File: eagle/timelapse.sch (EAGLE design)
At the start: 21 parts, among them Q1 200mA/40V, Q2 60V/32A/35mΩ, U2 TSR_1-2450

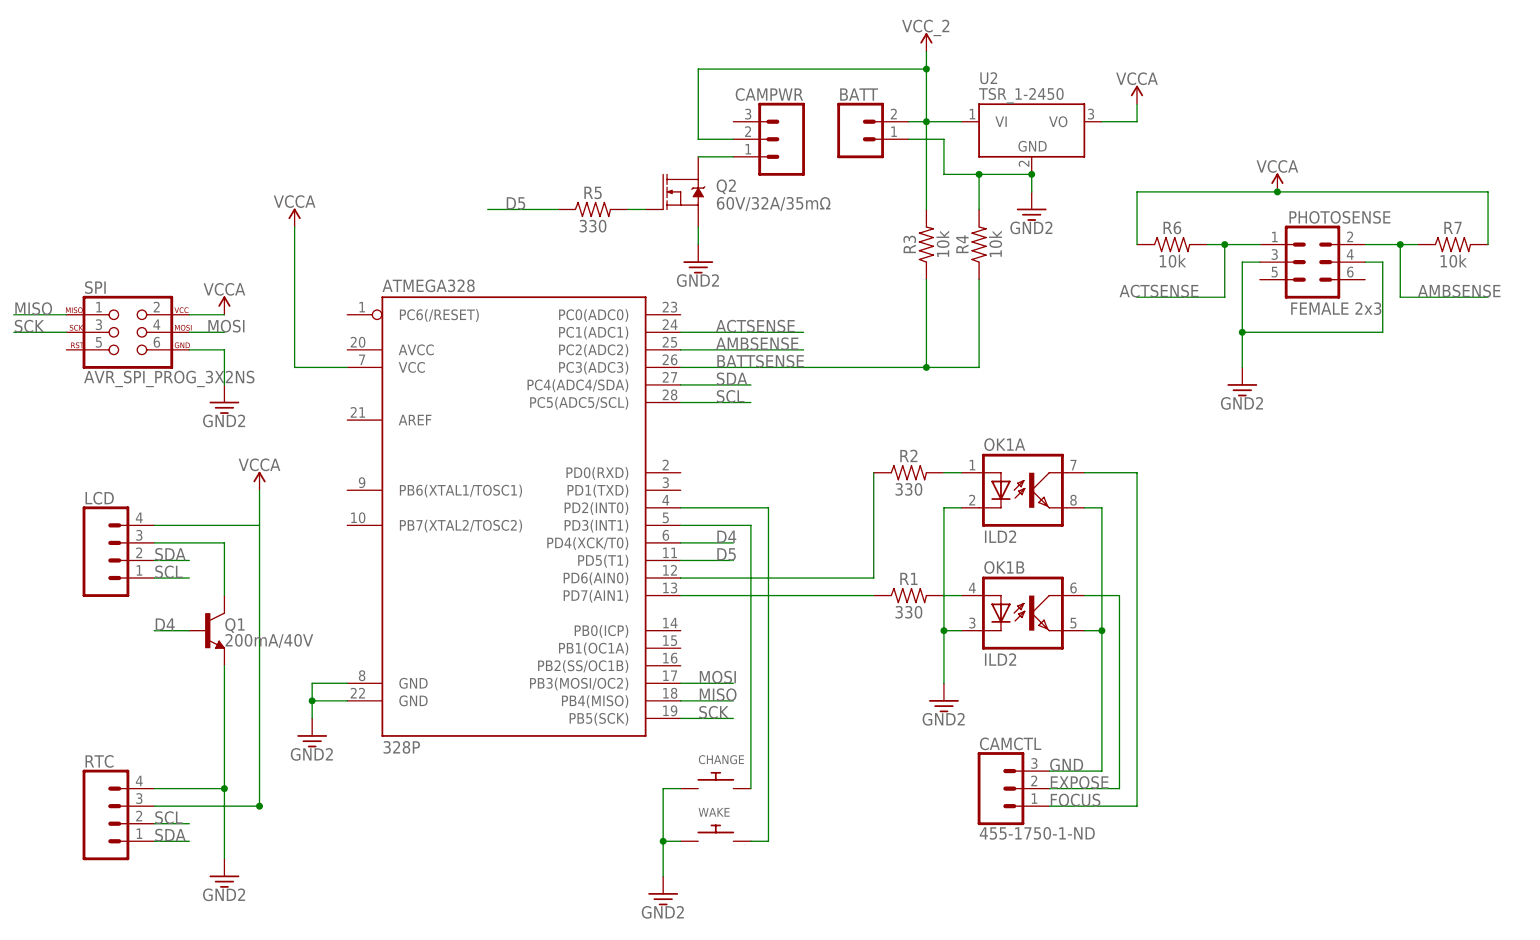
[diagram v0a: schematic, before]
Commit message: Remove old EAGLE files, fix missing wires in schema and add test points.
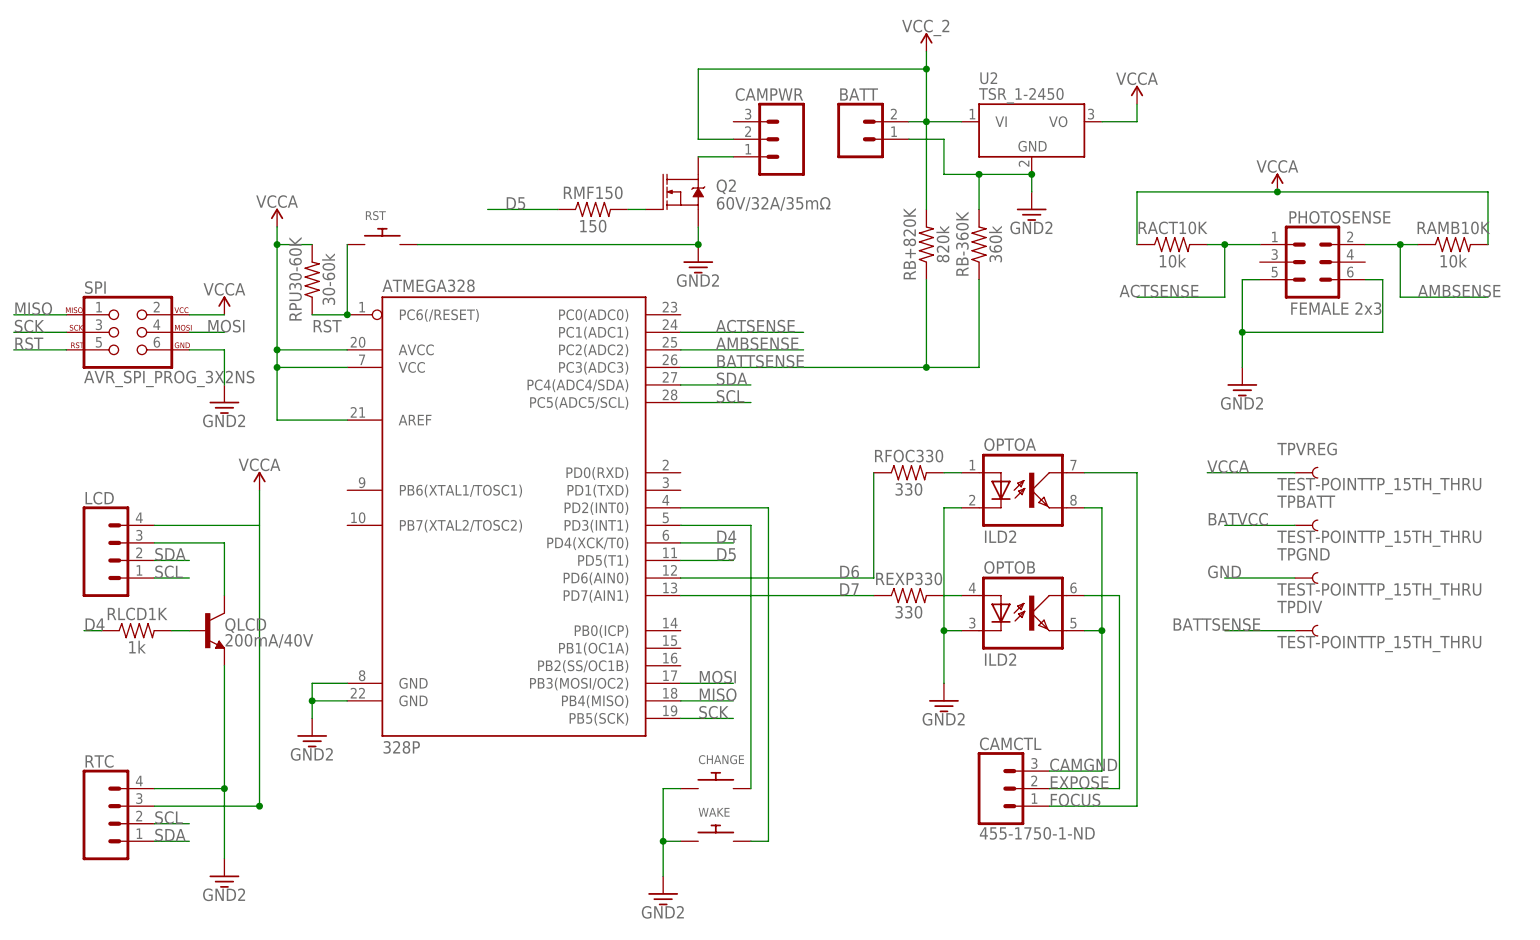
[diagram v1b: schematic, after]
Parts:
- added RLCD1K: 1k, SparkFun-Resistors:330OHM-HORIZ-1/10W-5%
- added RPU30-60K: 30-60k, SparkFun-Resistors:330OHM-HORIZ-1/10W-5%
- added RST: (no value), adafruit:SWITCH_PUSHBUTTONEVQ-PE
- added TPBATT, TPDIV, TPGND, TPVREG: TEST-POINTTP_15TH_THRU, SparkFun-Connectors:TEST-POINTTP_15TH_THRU
- RB+820K: value 10k -> 820k
- RB-360K: value 10k -> 360k
- RMF150: value 330 -> 150
- renumbered OK1 to OPTO, Q1 to QLCD, R1 to REXP330, R2 to RFOC330, R3 to RB+820K, R4 to RB-360K, R5 to RMF150, R6 to RACT10K, R7 to RAMB10K
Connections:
- net N$3 renamed D7
- net N$4 renamed D6
- removed net 3.3V: ATMEGA328.GND@1, ATMEGA328.GND@2, BATT.1, CHANGE.P$1, OPTOA.C, OPTOB.C, PHOTOSENSE.3, PHOTOSENSE.4, Q2.S, QLCD.E, RB-360K.2, RTC.4, SPI.6, U2.GND, WAKE.P$1
- removed net VCC2: BATT.2, CAMPWR.2, RB+820K.2, U2.VI
- new net BATVCC: BATT.2, CAMPWR.2, RB+820K.2, TPBATT.1, U2.VI
- new net CAMGND: CAMCTL.3, OPTOA.EMIT, OPTOB.EMIT
- new net N$3: QLCD.B, RLCD1K.2
- new net RST: ATMEGA328.PC6(/RESET), RPU30-60K.1, RST.P$1, SPI.5
- net BATTSENSE: now also TPDIV.1
- net D4: now also RLCD1K.1; no longer QLCD.B
- net GND: now also ATMEGA328.GND@1, ATMEGA328.GND@2, BATT.1, CHANGE.P$1, OPTOA.C, OPTOB.C, PHOTOSENSE.5, PHOTOSENSE.6, Q2.S, QLCD.E, RB-360K.2, RST.P$2, RTC.4, SPI.6, TPGND.1, U2.GND, WAKE.P$1; no longer CAMCTL.3, OPTOA.EMIT, OPTOB.EMIT
- net VCCA: now also ATMEGA328.AREF, ATMEGA328.AVCC, RPU30-60K.2, TPVREG.1
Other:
- note added: "Battery Input Max. 16V for 5V AREF"
- note added: "Photocells: Bright = ~100Ω Light = ~10kΩ Dark = ~50kΩ-1MΩ"

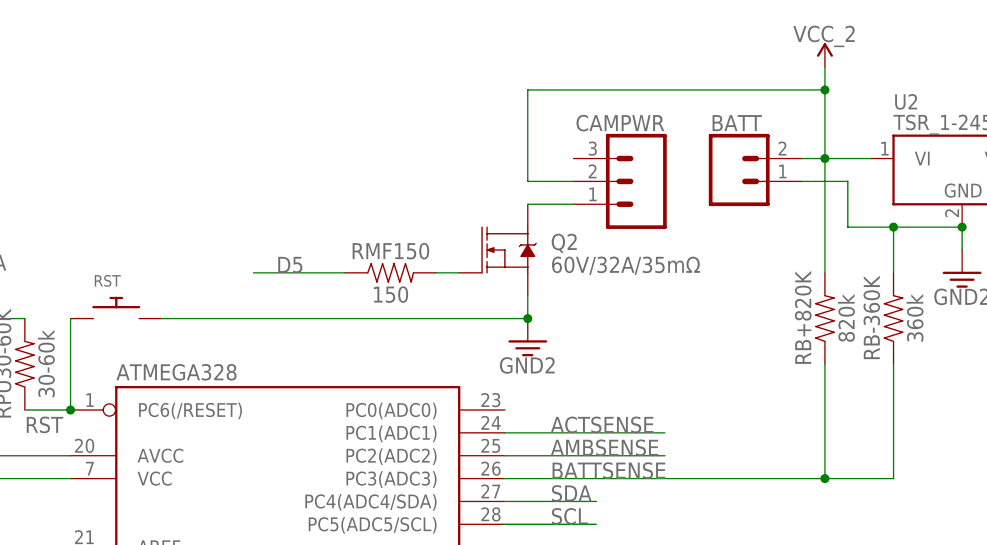
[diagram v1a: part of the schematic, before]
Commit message: Add capacitor for camera power supply.
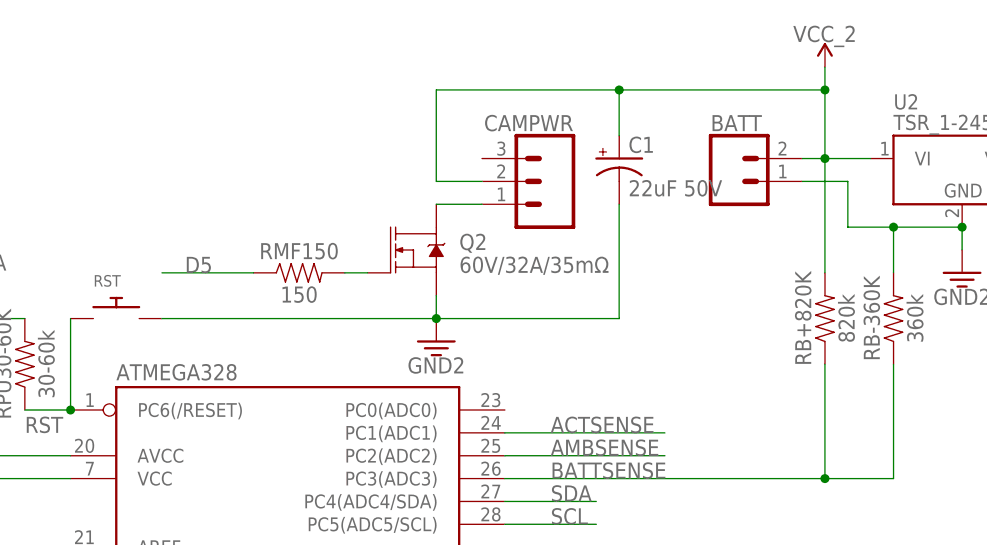
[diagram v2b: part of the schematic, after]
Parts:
- added C1: 22uF 50V, SparkFun-Capacitors:10UF-POLAR-RADIAL-2.5MM-25V-20%
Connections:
- net BATVCC: now also C1.+
- net GND: now also C1.-
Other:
- moved on the sheet: CAMPWR, Q2, RMF150
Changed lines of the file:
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@@
 <part name="TPDIV" library="SparkFun-Connectors" deviceset="TEST-POINT" device="TP_15TH_THRU"/>
 <part name="TPVREG" library="SparkFun-Connectors" deviceset="TEST-POINT" device="TP_15TH_THRU"/>
+<part name="C1" library="SparkFun-Capacitors" deviceset="10UF-POLAR" device="-RADIAL-2.5MM-25V-20%" value="22uF 50V"/>
 </parts>
 <sheets>
@@
 <instance part="RB+820K" gate="G$1" x="106.68" y="93.98" rot="R90"/>
 <instance part="RB-360K" gate="G$1" x="114.3" y="93.98" rot="R90"/>
-<instance part="Q2" gate="NMOS" x="71.12" y="101.6"/>
-<instance part="RMF150" gate="G$1" x="58.42" y="99.06"/>
+<instance part="Q2" gate="NMOS" x="60.96" y="101.6"/>
+<instance part="RMF150" gate="G$1" x="48.26" y="99.06"/>
 <instance part="BATTSUPPLY" gate="G$1" x="106.68" y="121.92"/>
-<instance part="SUPPLY6" gate="GND" x="73.66" y="91.44"/>
+<instance part="SUPPLY6" gate="GND" x="63.5" y="91.44"/>
 <instance part="PHOTOSENSE" gate="G$1" x="162.56" y="91.44"/>
 <instance part="SUPPLY7" gate="GND" x="152.4" y="73.66"/>
@@
 <instance part="WAKE" gate="G$1" x="76.2" y="7.62"/>
 <instance part="SUPPLY8" gate="GND" x="68.58" y="0"/>
-<instance part="CAMPWR" gate="J$1" x="86.36" y="109.22" rot="MR0"/>
+<instance part="CAMPWR" gate="J$1" x="76.2" y="109.22" rot="MR0"/>
 <instance part="OPTO" gate="A" x="121.92" y="58.42"/>
 <instance part="OPTO" gate="B" x="121.92" y="40.64"/>
@@
 <instance part="TPDIV" gate="G$1" x="160.02" y="38.1"/>
 <instance part="TPVREG" gate="G$1" x="160.02" y="60.96"/>
+<instance part="C1" gate="G$1" x="83.82" y="111.76"/>
 </instances>
 <busses>
@@
 <pinref part="Q2" gate="NMOS" pin="S"/>
 <pinref part="SUPPLY6" gate="GND" pin="3.3V"/>
-<wire x1="73.66" y1="96.52" x2="73.66" y2="93.98" width="0.1524" layer="91"/>
+<wire x1="63.5" y1="96.52" x2="63.5" y2="93.98" width="0.1524" layer="91"/>
 <pinref part="RST" gate="G$1" pin="P$2"/>
-<wire x1="33.02" y1="93.98" x2="73.66" y2="93.98" width="0.1524" layer="91"/>
-<junction x="73.66" y="93.98"/>
+<wire x1="33.02" y1="93.98" x2="63.5" y2="93.98" width="0.1524" layer="91"/>
+<junction x="63.5" y="93.98"/>
+<pinref part="C1" gate="G$1" pin="-"/>
+<wire x1="83.82" y1="106.68" x2="83.82" y2="93.98" width="0.1524" layer="91"/>
+<wire x1="83.82" y1="93.98" x2="63.5" y2="93.98" width="0.1524" layer="91"/>
 </segment>
 <segment>
@@
 <pinref part="CAMPWR" gate="J$1" pin="2"/>
 <wire x1="106.68" y1="119.38" x2="106.68" y2="121.92" width="0.1524" layer="91"/>
-<wire x1="78.74" y1="109.22" x2="73.66" y2="109.22" width="0.1524" layer="91"/>
-<wire x1="73.66" y1="109.22" x2="73.66" y2="119.38" width="0.1524" layer="91"/>
-<wire x1="73.66" y1="119.38" x2="106.68" y2="119.38" width="0.1524" layer="91"/>
+<wire x1="68.58" y1="109.22" x2="63.5" y2="109.22" width="0.1524" layer="91"/>
+<wire x1="63.5" y1="109.22" x2="63.5" y2="119.38" width="0.1524" layer="91"/>
+<wire x1="63.5" y1="119.38" x2="83.82" y2="119.38" width="0.1524" layer="91"/>
 <junction x="106.68" y="119.38"/>
+<pinref part="C1" gate="G$1" pin="+"/>
+<wire x1="83.82" y1="119.38" x2="106.68" y2="119.38" width="0.1524" layer="91"/>
+<wire x1="83.82" y1="114.3" x2="83.82" y2="119.38" width="0.1524" layer="91"/>
+<junction x="83.82" y="119.38"/>
 </segment>
 <segment>
@@
 <pinref part="Q2" gate="NMOS" pin="G"/>
 <pinref part="RMF150" gate="G$1" pin="2"/>
-<wire x1="66.04" y1="99.06" x2="63.5" y2="99.06" width="0.1524" layer="91"/>
+<wire x1="55.88" y1="99.06" x2="53.34" y2="99.06" width="0.1524" layer="91"/>
 </segment>
 </net>
@@
 <pinref part="Q2" gate="NMOS" pin="D"/>
 <pinref part="CAMPWR" gate="J$1" pin="1"/>
-<wire x1="73.66" y1="106.68" x2="78.74" y2="106.68" width="0.1524" layer="91"/>
+<wire x1="63.5" y1="106.68" x2="68.58" y2="106.68" width="0.1524" layer="91"/>
 </segment>
 </net>
@@
 <segment>
 <pinref part="RMF150" gate="G$1" pin="1"/>
-<wire x1="43.18" y1="99.06" x2="53.34" y2="99.06" width="0.1524" layer="91"/>
-<label x="45.72" y="99.06" size="1.778" layer="95"/>
-</segment>
-</net>
+<wire x1="33.02" y1="99.06" x2="43.18" y2="99.06" width="0.1524" layer="91"/>
+<label x="35.56" y="99.06" size="1.778" layer="95"/>
+</segment>
+</net>
